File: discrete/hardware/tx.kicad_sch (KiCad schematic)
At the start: 23 parts, among them Q10 2N5401, Q11 2N5551, Q12 2N5401, Q7 2N5551, Q8 2N5401, Q9 2N5551

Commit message: Begin multi-sheet
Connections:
- net OUT renamed RS232_OUT
- net TTO renamed DEC_TTO_232
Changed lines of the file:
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@@
-		)
-	)
-	(label "OUT"
-		(at 247.65 86.36 0)
-		(effects
-			(font
-				(size 1.27 1.27)
-			)
-			(justify left bottom)
 		)
 	)
@@
 		)
 	)
-	(label "TTO"
-		(at 48.26 88.9 0)
+	(hierarchical_label "DEC_TTO_232"
+		(shape input)
+		(at 45.72 88.9 180)
 		(effects
 			(font
 				(size 1.27 1.27)
 			)
-			(justify left bottom)
+			(justify right)
 		)
 	)
+	(hierarchical_label "RS232_OUT"
+		(shape output)
+		(at 255.27 86.36 0)
+		(effects
+			(font
+				(size 1.27 1.27)
+			)
+			(justify left)
+		)
+	)

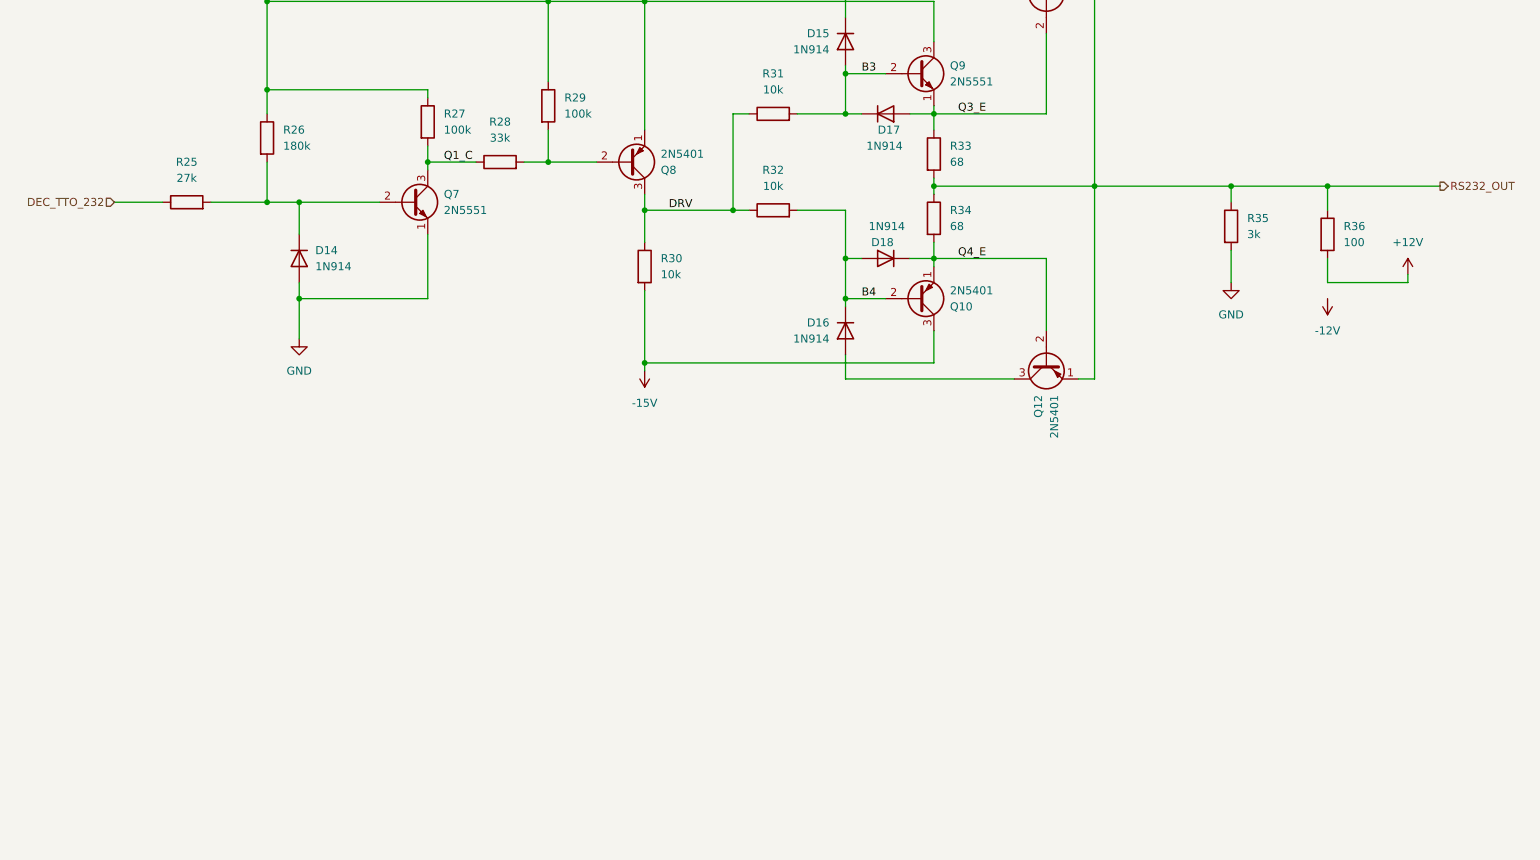
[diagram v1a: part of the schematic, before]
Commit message: Laid out full schematic. Added decoupling and test points
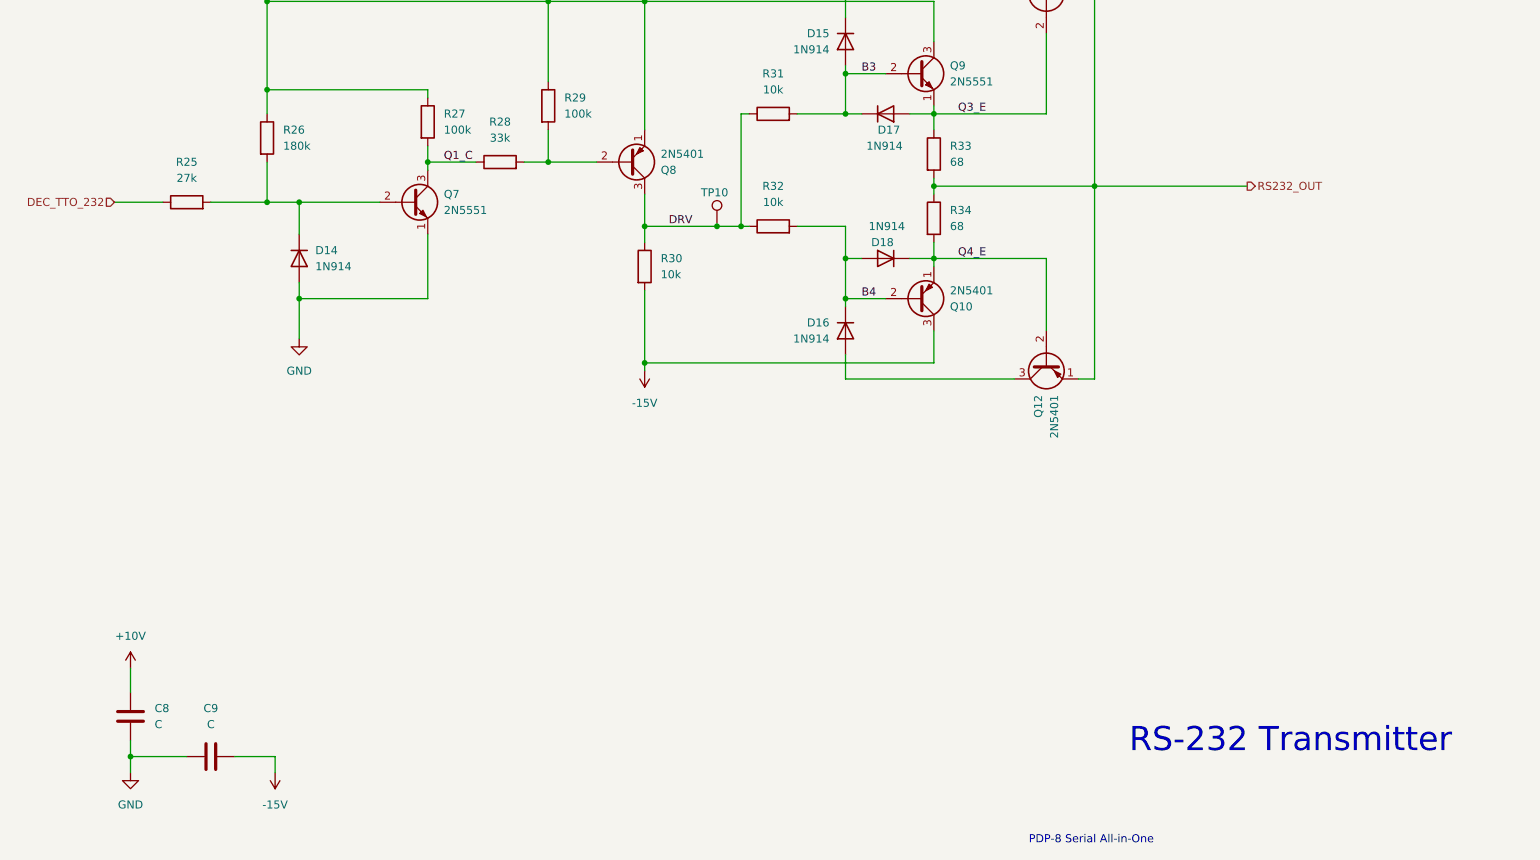
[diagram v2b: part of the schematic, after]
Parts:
- removed R35: 3k, symbol Device:R
- removed R36: 100, symbol Device:R
- added C8, C9: C, symbol Device:C
- added TP10: TestPoint, TestPoint:TestPoint_Loop_D3.50mm_Drill0.9mm_Beaded, symbol Connector:TestPoint
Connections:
- net +10V: now also C8.1
- net -15V: now also C9.2
- net DRV: now also TP10.1
- net GND: now also C8.2, C9.1
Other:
- note added: "PDP-8 Serial All-in-One"
- note added: "RS-232 Transmitter"
- moved on the sheet: R32

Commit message: Update transmitter with inverter and W050 handling
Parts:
- added DW1, DW2: 1N914, Diode_THT:D_DO-35_SOD27_P7.62mm_Horizontal, symbol Diode:1N914
- added I1: 90m, symbol Simulation_SPICE:IDC
- added J4: Conn_01x03, symbol Connector_Generic:Conn_01x03
- added QW1, QW2: 2N5401, Package_TO_SOT_THT:TO-92_Inline, symbol Transistor_BJT:2N3906
- added RW1: 1k8, symbol Device:R
- added RW2: 15k, symbol Device:R
- added RW3: 7k5, symbol Device:R
- added RW4: 47k, symbol Device:R
- added RW5: 100k, symbol Device:R
- added RW6: 10k, symbol Device:R
- C8, C9: value C -> 100nF
- R26: value 180k -> 47k
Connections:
- net +10V: now also RW5.2
- net -15V: now also I1.2, RW2.1, RW3.1, RW6.2
- net DEC_TTO_232: now also J4.3 (Pin_3), RW3.2, RW4.1; no longer R25.1
- net GND: now also DW1.2 (A), DW2.1 (K), QW2.1 (E)
- new net: DW1.1 (K), I1.1, QW1.1 (E)
- new net: J4.2 (Pin_2), R25.1
- new net: DW2.2 (A), QW2.2 (B), RW4.2, RW5.1
- new net: QW1.2 (B), RW1.2
- new net TTO_INV: J4.1 (Pin_1), QW2.3 (C), RW6.1
- new net W050_IN: RW1.1, RW2.2
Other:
- moved on the sheet: D14, D15, D16, D17, D18, Q10, Q11, Q12, Q7, Q8, Q9, R25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
